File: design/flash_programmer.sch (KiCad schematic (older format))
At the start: 0 parts

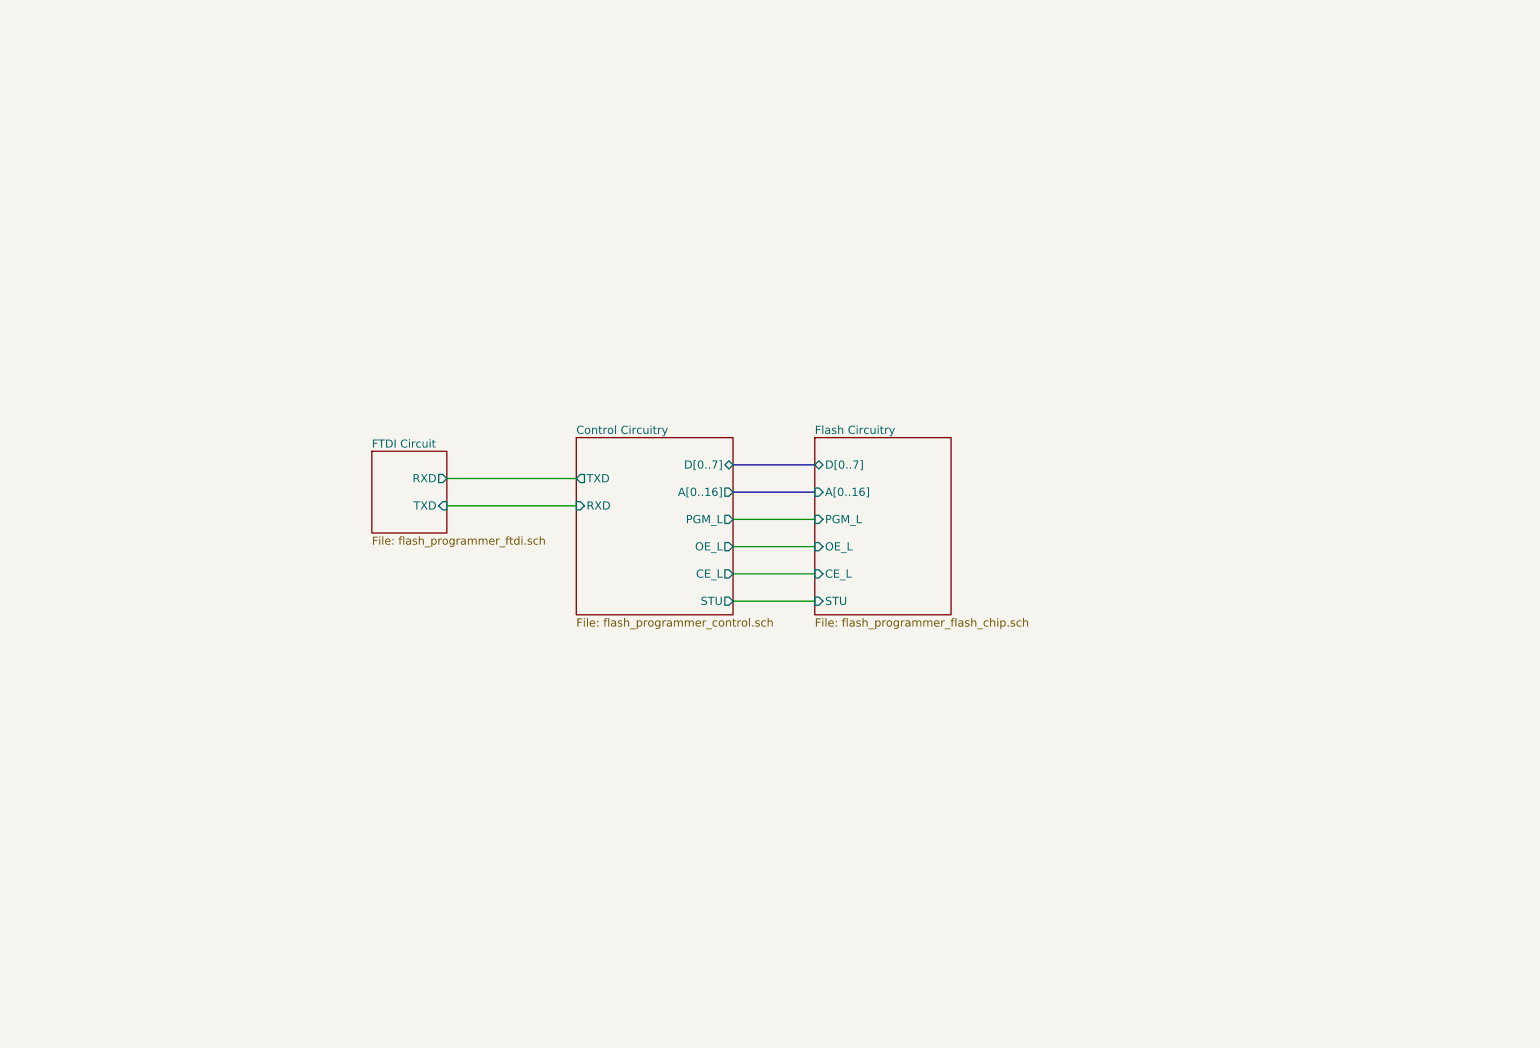
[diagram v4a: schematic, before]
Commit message: Bug fix and more schematic cleanup
The A9_VPP circuit wouldn't work in all cases, so I completely redid it and
it's simpler now.

Also started splitting up the schematic into even more sheets, and sprinkled in
some TODO comments.
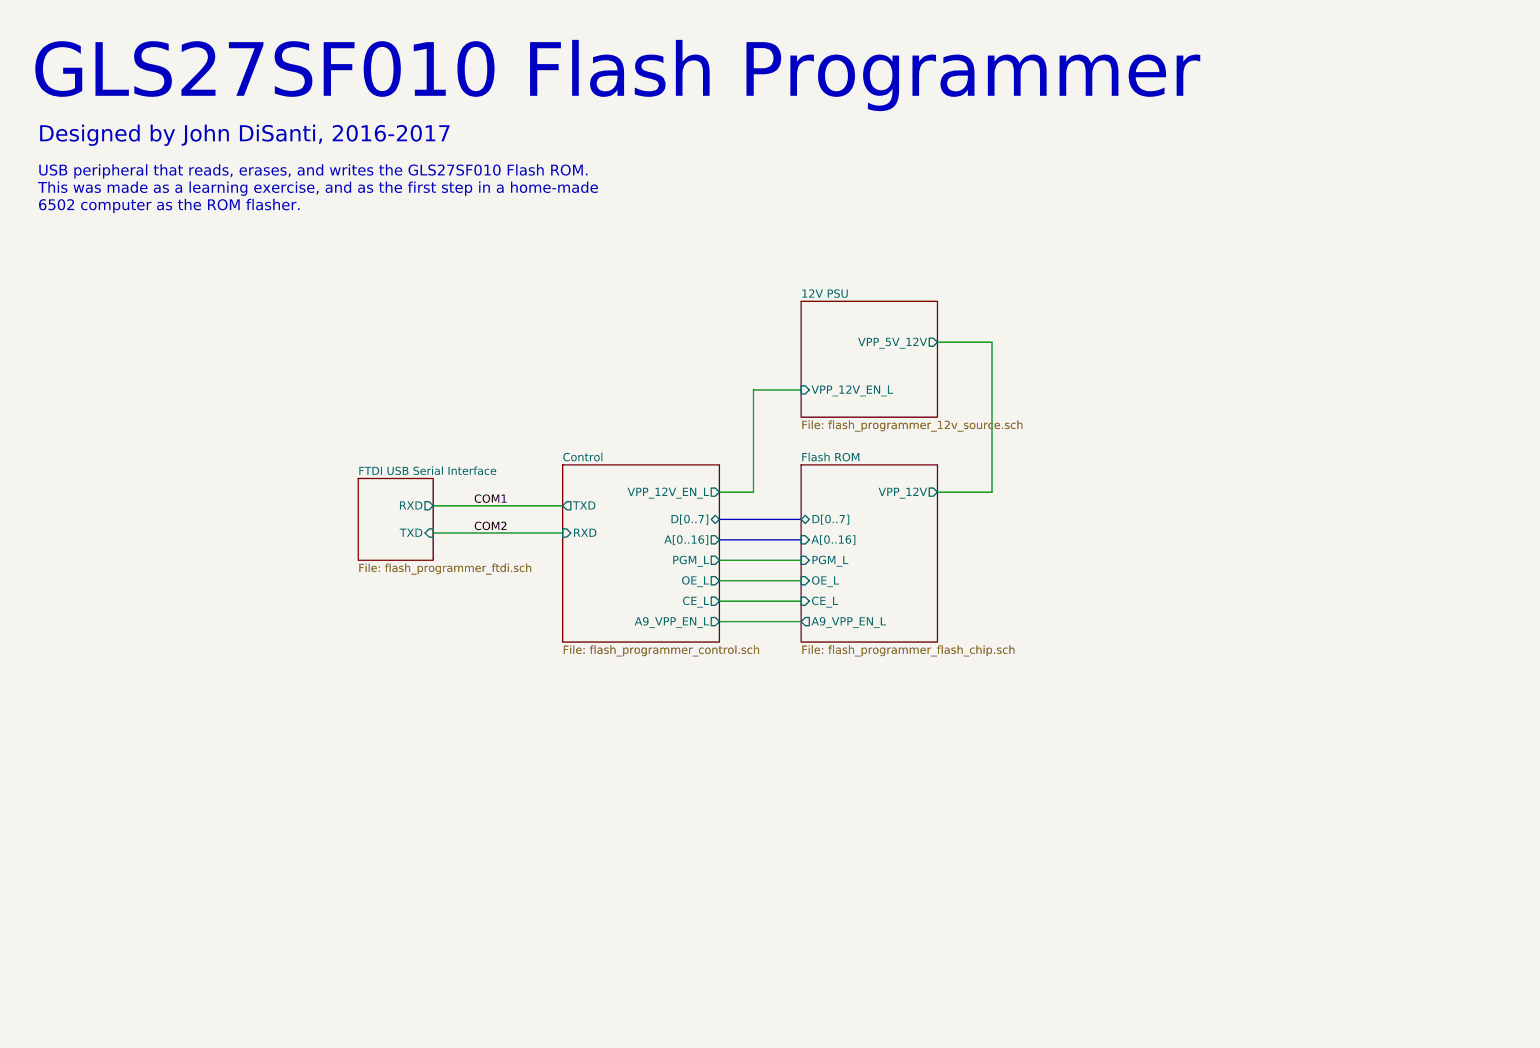
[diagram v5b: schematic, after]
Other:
- note added: "Designed by John DiSanti, 2016-2017"
- note added: "GLS27SF010 Flash Programmer"
- note added: "USB peripheral that reads, erases, and writes the GLS27SF010 Flash ROM.\nThis was made as a learning exercise, and as the first step in a home-made\n6502 computer as the ROM flasher."
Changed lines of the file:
@@
 $Descr USLetter 11000 8500
 encoding utf-8
-Sheet 1 4
-Title "Flash ROM Programmer for GLS27SF010"
-Date "2017-02-12"
-Rev "4"
+Sheet 1 5
+Title "GLS27SF010 Flash Programmer"
+Date "2017-03-11"
+Rev "5"
 Comp "John DiSanti"
 Comment1 ""
@@
 $EndDescr
 $Sheet
-S 3150 3700 550  600
+S 3050 3900 550  600
 U 58665314
-F0 "FTDI Circuit" 59
+F0 "FTDI USB Serial Interface" 59
 F1 "flash_programmer_ftdi.sch" 59
-F2 "RXD" O R 3700 3900 60
-F3 "TXD" I R 3700 4100 60
+F2 "RXD" O R 3600 4100 60
+F3 "TXD" I R 3600 4300 60
 $EndSheet
 Wire Wire Line
-	3700 3900 4650 3900
+	3600 4100 4550 4100
 Wire Wire Line
-	3700 4100 4650 4100
+	3600 4300 4550 4300
 $Sheet
-S 4650 3600 1150 1300
+S 4550 3800 1150 1300
 U 58C243E5
-F0 "Control Circuitry" 60
+F0 "Control" 60
 F1 "flash_programmer_control.sch" 60
-F2 "RXD" I L 4650 4100 60
-F3 "TXD" O L 4650 3900 60
-F4 "D[0..7]" B R 5800 3800 60
-F5 "A[0..16]" O R 5800 4000 60
-F6 "PGM_L" O R 5800 4200 60
-F7 "OE_L" O R 5800 4400 60
-F8 "CE_L" O R 5800 4600 60
-F9 "STU" O R 5800 4800 60
+F2 "RXD" I L 4550 4300 60
+F3 "TXD" O L 4550 4100 60
+F4 "D[0..7]" B R 5700 4200 60
+F5 "A[0..16]" O R 5700 4350 60
+F6 "PGM_L" O R 5700 4500 60
+F7 "OE_L" O R 5700 4650 60
+F8 "CE_L" O R 5700 4800 60
+F9 "VPP_12V_EN_L" O R 5700 4000 60
+F10 "A9_VPP_EN_L" O R 5700 4950 60
 $EndSheet
 $Sheet
-S 6400 3600 1000 1300
+S 6300 3800 1000 1300
 U 58BA78AE
-F0 "Flash Circuitry" 60
+F0 "Flash ROM" 60
 F1 "flash_programmer_flash_chip.sch" 60
-F2 "A[0..16]" I L 6400 4000 60
-F3 "D[0..7]" B L 6400 3800 60
-F4 "OE_L" I L 6400 4400 60
-F5 "STU" I L 6400 4800 60
-F6 "CE_L" I L 6400 4600 60
-F7 "PGM_L" I L 6400 4200 60
+F2 "A[0..16]" I L 6300 4350 60
+F3 "D[0..7]" B L 6300 4200 60
+F4 "OE_L" I L 6300 4650 60
+F5 "CE_L" I L 6300 4800 60
+F6 "PGM_L" I L 6300 4500 60
+F7 "VPP_12V" O R 7300 4000 60
+F8 "A9_VPP_EN_L" O L 6300 4950 60
 $EndSheet
+Text Label 3900 4100 0    60   ~ 0
+COM1
+Text Label 3900 4300 0    60   ~ 0
+COM2
+$Sheet
+S 6300 2600 1000 850
+U 58C44875
+F0 "12V PSU" 60
+F1 "flash_programmer_12v_source.sch" 60
+F2 "VPP_12V_EN_L" I L 6300 3250 60
+F3 "VPP_5V_12V" O R 7300 2900 60
+$EndSheet
+Wire Wire Line
+	5700 4000 5950 4000
+Wire Wire Line
+	5950 4000 5950 3250
+Wire Wire Line
+	5950 3250 6300 3250
 Wire Bus Line
-	5800 3800 6400 3800
+	5700 4200 6300 4200
 Wire Bus Line
-	5800 4000 6400 4000
+	5700 4350 6300 4350
 Wire Wire Line
-	5800 4200 6400 4200
+	5700 4500 6300 4500
 Wire Wire Line
-	5800 4400 6400 4400
+	5700 4650 6300 4650
 Wire Wire Line
-	5800 4600 6400 4600
+	5700 4800 6300 4800
 Wire Wire Line
-	5800 4800 6400 4800
+	5700 4950 6300 4950
+Wire Wire Line
+	7300 2900 7700 2900
+Wire Wire Line
+	7700 2900 7700 4000
+Wire Wire Line
+	7700 4000 7300 4000
+Text Notes 650  1150 0    394  ~ 0
+GLS27SF010 Flash Programmer
+Text Notes 700  1450 0    118  ~ 0
+Designed by John DiSanti, 2016-2017
+Text Notes 700  1950 0    79   ~ 0
+USB peripheral that reads, erases, and writes the GLS27SF010 Flash ROM.\nThis was made as a learning exercise, and as the first step in a home-made\n6502 computer as the ROM flasher.
 $EndSCHEMATC

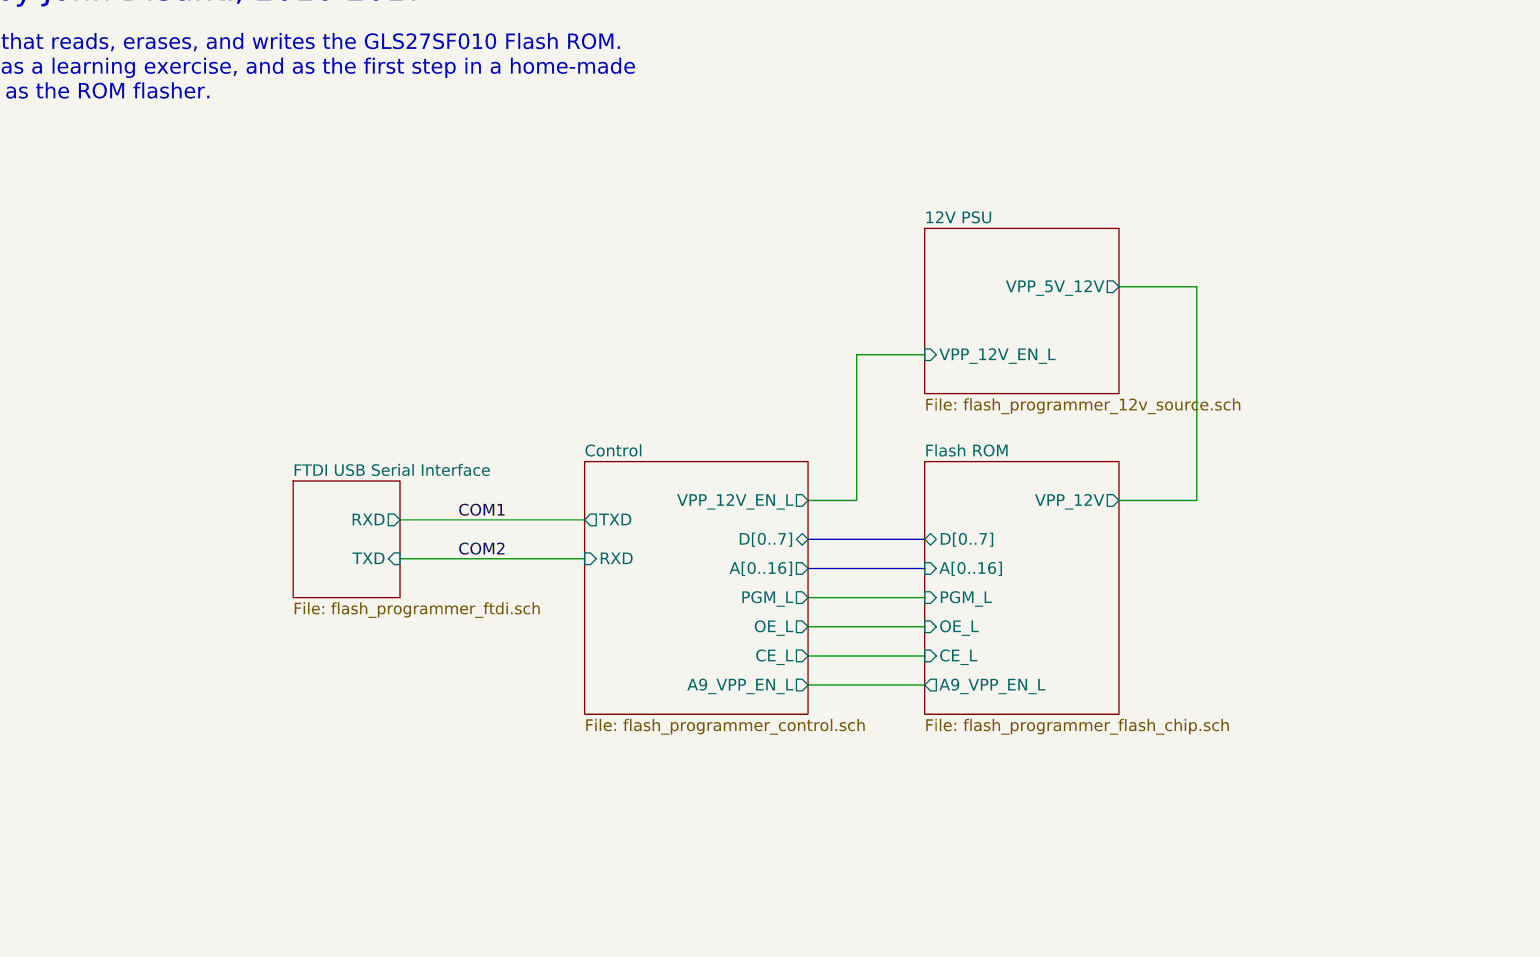
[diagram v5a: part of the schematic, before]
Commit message: More schematic clean up
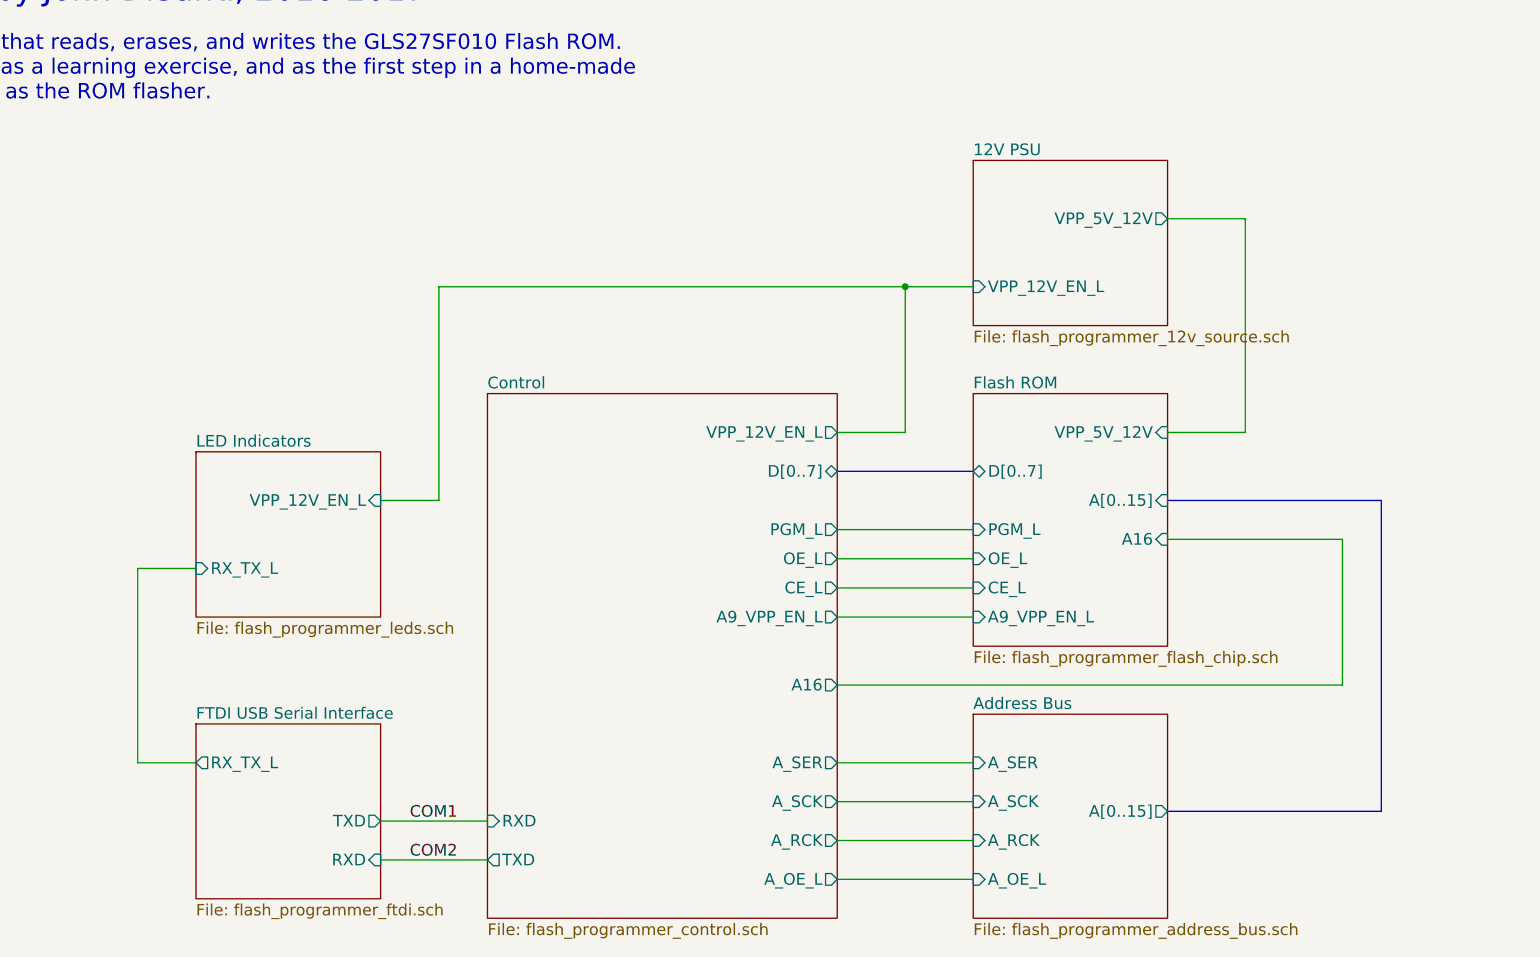
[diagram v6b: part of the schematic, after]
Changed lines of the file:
@@
 EESchema Schematic File Version 2
 LIBS:gls27sf010
+LIBS:atmega328p
 LIBS:flash_programmer
 LIBS:power
@@
 $Descr USLetter 11000 8500
 encoding utf-8
-Sheet 1 5
+Sheet 1 7
 Title "GLS27SF010 Flash Programmer"
 Date "2017-03-11"
@@
 $EndDescr
 $Sheet
-S 3050 3900 550  600
+S 2550 5150 950  900
 U 58665314
 F0 "FTDI USB Serial Interface" 59
 F1 "flash_programmer_ftdi.sch" 59
-F2 "RXD" O R 3600 4100 60
-F3 "TXD" I R 3600 4300 60
+F2 "RXD" I R 3500 5850 60
+F3 "TXD" O R 3500 5650 60
+F4 "RX_TX_L" O L 2550 5350 60
 $EndSheet
 Wire Wire Line
-	3600 4100 4550 4100
+	3500 5650 4050 5650
 Wire Wire Line
-	3600 4300 4550 4300
+	3500 5850 4050 5850
 $Sheet
-S 4550 3800 1150 1300
-U 58C243E5
-F0 "Control" 60
-F1 "flash_programmer_control.sch" 60
-F2 "RXD" I L 4550 4300 60
-F3 "TXD" O L 4550 4100 60
-F4 "D[0..7]" B R 5700 4200 60
-F5 "A[0..16]" O R 5700 4350 60
-F6 "PGM_L" O R 5700 4500 60
-F7 "OE_L" O R 5700 4650 60
-F8 "CE_L" O R 5700 4800 60
-F9 "VPP_12V_EN_L" O R 5700 4000 60
-F10 "A9_VPP_EN_L" O R 5700 4950 60
-$EndSheet
-$Sheet
-S 6300 3800 1000 1300
+S 6550 3450 1000 1300
 U 58BA78AE
 F0 "Flash ROM" 60
 F1 "flash_programmer_flash_chip.sch" 60
-F2 "A[0..16]" I L 6300 4350 60
-F3 "D[0..7]" B L 6300 4200 60
-F4 "OE_L" I L 6300 4650 60
-F5 "CE_L" I L 6300 4800 60
-F6 "PGM_L" I L 6300 4500 60
-F7 "VPP_12V" O R 7300 4000 60
-F8 "A9_VPP_EN_L" O L 6300 4950 60
+F2 "OE_L" I L 6550 4300 60
+F3 "CE_L" I L 6550 4450 60
+F4 "PGM_L" I L 6550 4150 60
+F5 "A16" I R 7550 4200 60
+F6 "A[0..15]" I R 7550 4000 60
+F7 "D[0..7]" B L 6550 3850 60
+F8 "A9_VPP_EN_L" I L 6550 4600 60
+F9 "VPP_5V_12V" I R 7550 3650 60
 $EndSheet
-Text Label 3900 4100 0    60   ~ 0
+Text Label 3650 5650 0    60   ~ 0
 COM1
-Text Label 3900 4300 0    60   ~ 0
+Text Label 3650 5850 0    60   ~ 0
 COM2
 $Sheet
-S 6300 2600 1000 850
+S 6550 2250 1000 850
 U 58C44875
 F0 "12V PSU" 60
 F1 "flash_programmer_12v_source.sch" 60
-F2 "VPP_12V_EN_L" I L 6300 3250 60
-F3 "VPP_5V_12V" O R 7300 2900 60
+F2 "VPP_12V_EN_L" I L 6550 2900 60
+F3 "VPP_5V_12V" O R 7550 2550 60
 $EndSheet
 Wire Wire Line
-	5700 4000 5950 4000
+	5850 3650 6200 3650
 Wire Wire Line
-	5950 4000 5950 3250
+	6200 3650 6200 2900
 Wire Wire Line
-	5950 3250 6300 3250
+	3800 2900 6550 2900
 Wire Bus Line
-	5700 4200 6300 4200
-Wire Bus Line
-	5700 4350 6300 4350
+	5850 3850 6550 3850
 Wire Wire Line
-	5700 4500 6300 4500
+	5850 4150 6550 4150
 Wire Wire Line
-	5700 4650 6300 4650
+	5850 4300 6550 4300
 Wire Wire Line
-	5700 4800 6300 4800
+	5850 4450 6550 4450
 Wire Wire Line
-	5700 4950 6300 4950
+	5850 4600 6550 4600
 Wire Wire Line
-	7300 2900 7700 2900
+	7550 2550 7950 2550
 Wire Wire Line
-	7700 2900 7700 4000
+	7950 2550 7950 3650
 Wire Wire Line
-	7700 4000 7300 4000
+	7950 3650 7550 3650
 Text Notes 650  1150 0    394  ~ 0
 GLS27SF010 Flash Programmer
@@
 Text Notes 700  1950 0    79   ~ 0
 USB peripheral that reads, erases, and writes the GLS27SF010 Flash ROM.\nThis was made as a learning exercise, and as the first step in a home-made\n6502 computer as the ROM flasher.
+$Sheet
+S 6550 5100 1000 1050
+U 58C678D4
+F0 "Address Bus" 60
+F1 "flash_programmer_address_bus.sch" 60
+F2 "A_SER" I L 6550 5350 60
+F3 "A_SCK" I L 6550 5550 60
+F4 "A_RCK" I L 6550 5750 60
+F5 "A_OE_L" I L 6550 5950 60
+F6 "A[0..15]" O R 7550 5600 60
+$EndSheet
+$Sheet
+S 4050 3450 1800 2700
+U 58C243E5
+F0 "Control" 60
+F1 "flash_programmer_control.sch" 60
+F2 "RXD" I L 4050 5650 60
+F3 "PGM_L" O R 5850 4150 60
+F4 "OE_L" O R 5850 4300 60
+F5 "CE_L" O R 5850 4450 60
+F6 "VPP_12V_EN_L" O R 5850 3650 60
+F7 "A9_VPP_EN_L" O R 5850 4600 60
+F8 "A_SCK" O R 5850 5550 60
+F9 "A_RCK" O R 5850 5750 60
+F10 "A_OE_L" O R 5850 5950 60
+F11 "A_SER" O R 5850 5350 60
+F12 "TXD" O L 4050 5850 60
+F13 "A16" O R 5850 4950 60
+F14 "D[0..7]" B R 5850 3850 60
+$EndSheet
+Wire Wire Line
+	5850 5350 6550 5350
+Wire Wire Line
+	5850 5550 6550 5550
+Wire Wire Line
+	5850 5750 6550 5750
+Wire Wire Line
+	5850 5950 6550 5950
+Wire Bus Line
+	7550 5600 8650 5600
+Wire Bus Line
+	8650 5600 8650 4000
+Wire Bus Line
+	8650 4000 7550 4000
+$Sheet
+S 2550 3750 950  850
+U 58C7589B
+F0 "LED Indicators" 60
+F1 "flash_programmer_leds.sch" 60
+F2 "VPP_12V_EN_L" I R 3500 4000 60
+F3 "RX_TX_L" I L 2550 4350 60
+$EndSheet
+Wire Wire Line
+	2550 5350 2250 5350
+Wire Wire Line
+	2250 5350 2250 4350
+Wire Wire Line
+	2250 4350 2550 4350
+Wire Wire Line
+	3500 4000 3800 4000
+Wire Wire Line
+	3800 4000 3800 2900
+Connection ~ 6200 2900
+Wire Wire Line
+	5850 4950 8450 4950
+Wire Wire Line
+	8450 4950 8450 4200
+Wire Wire Line
+	8450 4200 7550 4200
 $EndSCHEMATC
